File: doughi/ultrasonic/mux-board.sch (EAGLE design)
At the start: 34 parts, among them U1 TLV70233DBVR, X1 MINI-USB-UX60A-MB-5ST

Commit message: Made Schematic Neater
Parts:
- removed C8, C9: 1uF, rcl:C-USC0603
- removed POWER-LED: (no value), card:LEDSML0603
- removed R1: 10k, resistor:R-US_R0603
- removed R2: 1k, resistor:R-US_R0603
- removed SV1, SV10, SV11, SV12, SV13, SV14, SV15, SV16, SV2, SV3, SV4, SV5, SV6, SV7, SV8, SV9: (no value), mux-board:FE04-1
- removed U1: TLV70233DBVR, card:TLV70233DBVR
- added C10, C11: 1uF, rcl:C-USC0603
- added POWER-LED1: (no value), card:LEDSML0603
- added Q10, Q11, Q12, Q7, Q8, Q9: BSS138SMD, Logic_Level_Bidirectional:BSS138SMD
- added R15, R16, R17, R18, R19, R20, R21, R22, R23, R24, R25, R26: 10k, rcl:R-US_R0603
- added R3: 10k, resistor:R-US_R0603
- added R4: 1k, resistor:R-US_R0603
- added SV17, SV18, SV19, SV20, SV21, SV22, SV23, SV24, SV25, SV26, SV27, SV28, SV29, SV30, SV31, SV32: (no value), mux-board:FE04-1
- added U2: TLV70233DBVR, card:TLV70233DBVR
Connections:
- removed net N$3: R1.2, U1.EN
- removed net N$4: POWER-LED.C, R2.2
- new net ECHO_: Q12.S, R26.1, U$1.PA07/I7/AIN7/SERCOM0.3/I2SD0
- new net N$10: R3.2, U2.EN
- new net N$11: POWER-LED1.C, R4.2
- new net S0_: Q7.S, R16.1, U$1.PA02/EINT2/AIN0/Y0/VOUT
- new net S1_: Q8.S, R18.1, U$1.PA03/EINT3/VREFA/AIN1
- new net S2_: Q9.S, R20.1, U$1.PA04/EINT4/VREFB/AIN4/SERCOM0.0
- new net S3_: Q10.S, R22.1, U$1.PA05/EINT5/AIN5/SERCOM0.1
- new net TRIG_: Q11.S, R24.1, U$1.PA06/EINT6/AIN6/SERCOM0.2
- net +3.3V: now also C11.1, Q10.G, Q11.G, Q12.G, Q7.G, Q8.G, Q9.G, R16.2, R18.2, R20.2, R22.2, R24.2, R26.2, U2.VOUT; no longer C9.1, U1.VOUT
- net +5V: now also C10.1, POWER-LED1.A, R15.2, R17.2, R19.2, R21.2, R23.2, R25.2, R3.1, SV17.4, SV18.4, SV19.4, SV20.4, SV21.4, SV22.4, SV23.4, SV24.4, SV25.4, SV26.4, SV27.4, SV28.4, SV29.4, SV30.4, SV31.4, SV32.4, U2.VIN; no longer C8.1, POWER-LED.A, R1.1, SV1.4, SV10.4, SV11.4, SV12.4, SV13.4, SV14.4, SV15.4, SV16.4, SV2.4, SV3.4, SV4.4, SV5.4, SV6.4, SV7.4, SV8.4, SV9.4, U1.VIN
- net E0: now also SV17.2; no longer SV1.2
- net E1: now also SV18.2; no longer SV2.2
- net E10: now also SV27.2; no longer SV11.2
- net E11: now also SV28.2; no longer SV12.2
- net E12: now also SV29.2; no longer SV13.2
- net E13: now also SV30.2; no longer SV14.2
- net E14: now also SV31.2; no longer SV15.2
- net E15: now also SV32.2; no longer SV16.2
- net E2: now also SV19.2; no longer SV3.2
- net E3: now also SV20.2; no longer SV4.2
- net E4: now also SV21.2; no longer SV5.2
- net E5: now also SV22.2; no longer SV6.2
- net E6: now also SV23.2; no longer SV7.2
- net E7: now also SV24.2; no longer SV8.2
- net E8: now also SV25.2; no longer SV9.2
- net E9: now also SV26.2; no longer SV10.2
- net ECHO: now also Q12.D, R25.1; no longer U$1.PA07/I7/AIN7/SERCOM0.3/I2SD0
- net GND: now also C10.2, C11.2, R4.1, SV17.1, SV18.1, SV19.1, SV20.1, SV21.1, SV22.1, SV23.1, SV24.1, SV25.1, SV26.1, SV27.1, SV28.1, SV29.1, SV30.1, SV31.1, SV32.1, U2.GND; no longer C8.2, C9.2, R2.1, SV1.1, SV10.1, SV11.1, SV12.1, SV13.1, SV14.1, SV15.1, SV16.1, SV2.1, SV3.1, SV4.1, SV5.1, SV6.1, SV7.1, SV8.1, SV9.1, U1.GND
- net S0: now also Q7.D, R15.1; no longer U$1.PA02/EINT2/AIN0/Y0/VOUT
- net S1: now also Q8.D, R17.1; no longer U$1.PA03/EINT3/VREFA/AIN1
- net S2: now also Q9.D, R19.1; no longer U$1.PA04/EINT4/VREFB/AIN4/SERCOM0.0
- net S3: now also Q10.D, R21.1; no longer U$1.PA05/EINT5/AIN5/SERCOM0.1
- net T0: now also SV17.3; no longer SV1.3
- net T1: now also SV18.3; no longer SV2.3
- net T10: now also SV27.3; no longer SV11.3
- net T11: now also SV28.3; no longer SV12.3
- net T12: now also SV29.3; no longer SV13.3
- net T13: now also SV30.3; no longer SV14.3
- net T14: now also SV31.3; no longer SV15.3
- net T15: now also SV32.3; no longer SV16.3
- net T2: now also SV19.3; no longer SV3.3
- net T3: now also SV20.3; no longer SV4.3
- net T4: now also SV21.3; no longer SV5.3
- net T5: now also SV22.3; no longer SV6.3
- net T6: now also SV23.3; no longer SV7.3
- net T7: now also SV24.3; no longer SV8.3
- net T8: now also SV25.3; no longer SV9.3
- net T9: now also SV26.3; no longer SV10.3
- net TRIG: now also Q11.D, R23.1; no longer U$1.PA06/EINT6/AIN6/SERCOM0.2
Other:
- note added: "Level Shifters"
- note added: "Microcontroller"
- note added: "Multiplexors"
- note added: "Sensor Connectors"
- note added: "USB Connector"
- note added: "Voltage Regulator and Power Light"

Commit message: Ultrasonic Mux Board Pre-Review
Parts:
- removed C7: 10 uF, resistor:C-USC0603
- removed SV17, SV18, SV19, SV20, SV21, SV22, SV23, SV24, SV25, SV26, SV27, SV28, SV29, SV30, SV31, SV32: (no value), mux-board:FE04-1
- added C8: 1uF, rcl:C-USC0603
- added J1: B2P-VH(LF)(SN), RoboJackets-Connectors:B2P-VH(LF)(SN)
- added US1, US2, US3, US4, US5, US6, US7, US8: 4-PIN_2MM-H, RoboJackets-Connectors:4-PIN_2MM-H
- added US10, US11, US12, US13, US14, US15, US16, US9: 4-PIN_2MM-V, RoboJackets-Connectors:4-PIN_2MM-V
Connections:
- net +5V: now also C8.1, J1.1, US1.4, US10.4, US11.4, US12.4, US13.4, US14.4, US15.4, US16.4, US2.4, US3.4, US4.4, US5.4, US6.4, US7.4, US8.4, US9.4; no longer C7.1, SV17.4, SV18.4, SV19.4, SV20.4, SV21.4, SV22.4, SV23.4, SV24.4, SV25.4, SV26.4, SV27.4, SV28.4, SV29.4, SV30.4, SV31.4, SV32.4
- net E0: now also US1.2; no longer SV17.2
- net E1: now also US2.2; no longer SV18.2
- net E10: now also US11.2; no longer SV27.2
- net E11: now also US12.2; no longer SV28.2
- net E12: now also US13.2; no longer SV29.2
- net E13: now also US14.2; no longer SV30.2
- net E14: now also US15.2; no longer SV31.2
- net E15: now also US16.2; no longer SV32.2
- net E2: now also US3.2; no longer SV19.2
- net E3: now also US4.2; no longer SV20.2
- net E4: now also US5.2; no longer SV21.2
- net E5: now also US6.2; no longer SV22.2
- net E6: now also US7.2; no longer SV23.2
- net E7: now also US8.2; no longer SV24.2
- net E8: now also US9.2; no longer SV25.2
- net E9: now also US10.2; no longer SV26.2
- net GND: now also C8.2, J1.2, US1.1, US10.1, US11.1, US12.1, US13.1, US14.1, US15.1, US16.1, US2.1, US3.1, US4.1, US5.1, US6.1, US7.1, US8.1, US9.1; no longer C7.2, SV17.1, SV18.1, SV19.1, SV20.1, SV21.1, SV22.1, SV23.1, SV24.1, SV25.1, SV26.1, SV27.1, SV28.1, SV29.1, SV30.1, SV31.1, SV32.1
- net T0: now also US1.3; no longer SV17.3
- net T1: now also US2.3; no longer SV18.3
- net T10: now also US11.3; no longer SV27.3
- net T11: now also US12.3; no longer SV28.3
- net T12: now also US13.3; no longer SV29.3
- net T13: now also US14.3; no longer SV30.3
- net T14: now also US15.3; no longer SV31.3
- net T15: now also US16.3; no longer SV32.3
- net T2: now also US3.3; no longer SV19.3
- net T3: now also US4.3; no longer SV20.3
- net T4: now also US5.3; no longer SV21.3
- net T5: now also US6.3; no longer SV22.3
- net T6: now also US7.3; no longer SV23.3
- net T7: now also US8.3; no longer SV24.3
- net T8: now also US9.3; no longer SV25.3
- net T9: now also US10.3; no longer SV26.3
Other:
- note added: "Power Source/Indicator LED"
- note added: "Voltage Regulator"
- note removed: "Voltage Regulator and Power Light"
- moved on the sheet: C10, C11, POWER-LED1, R3, R4, U2

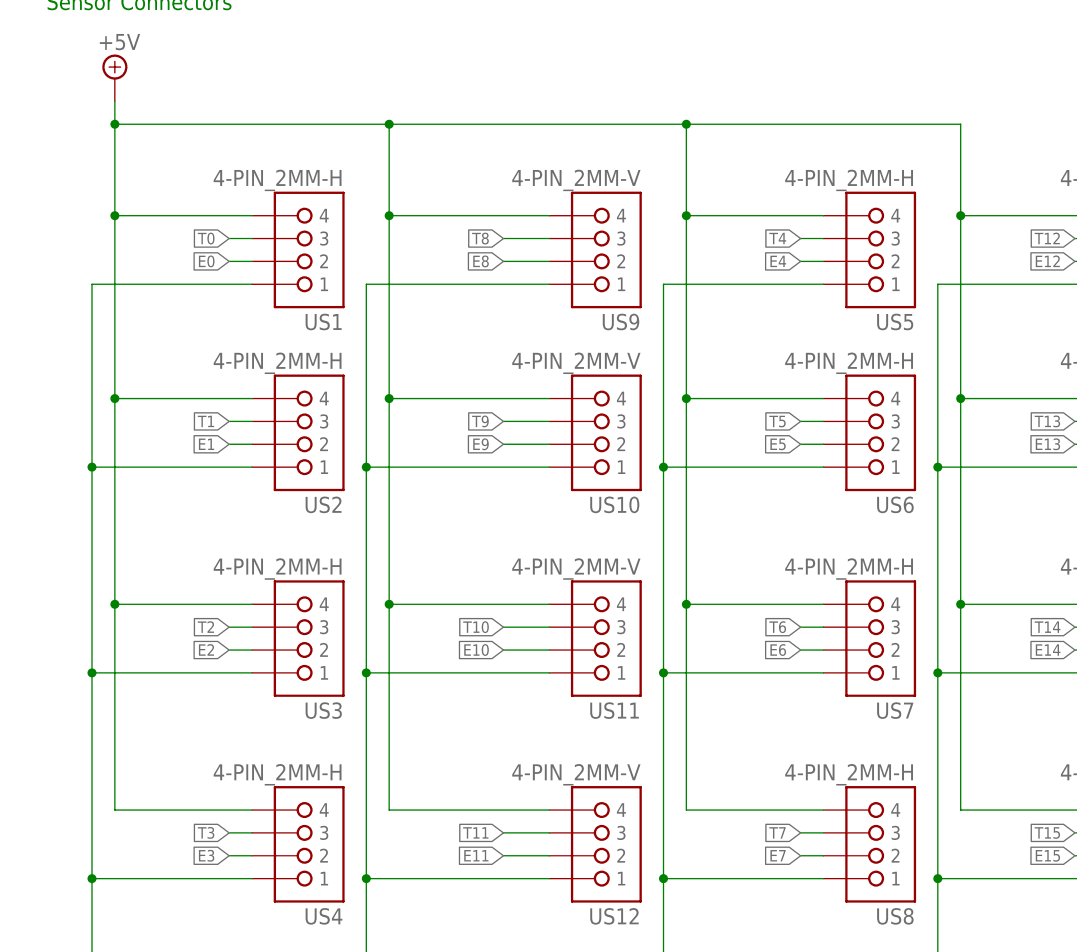
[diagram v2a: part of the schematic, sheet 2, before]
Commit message: Finished routing Ultrasonic board
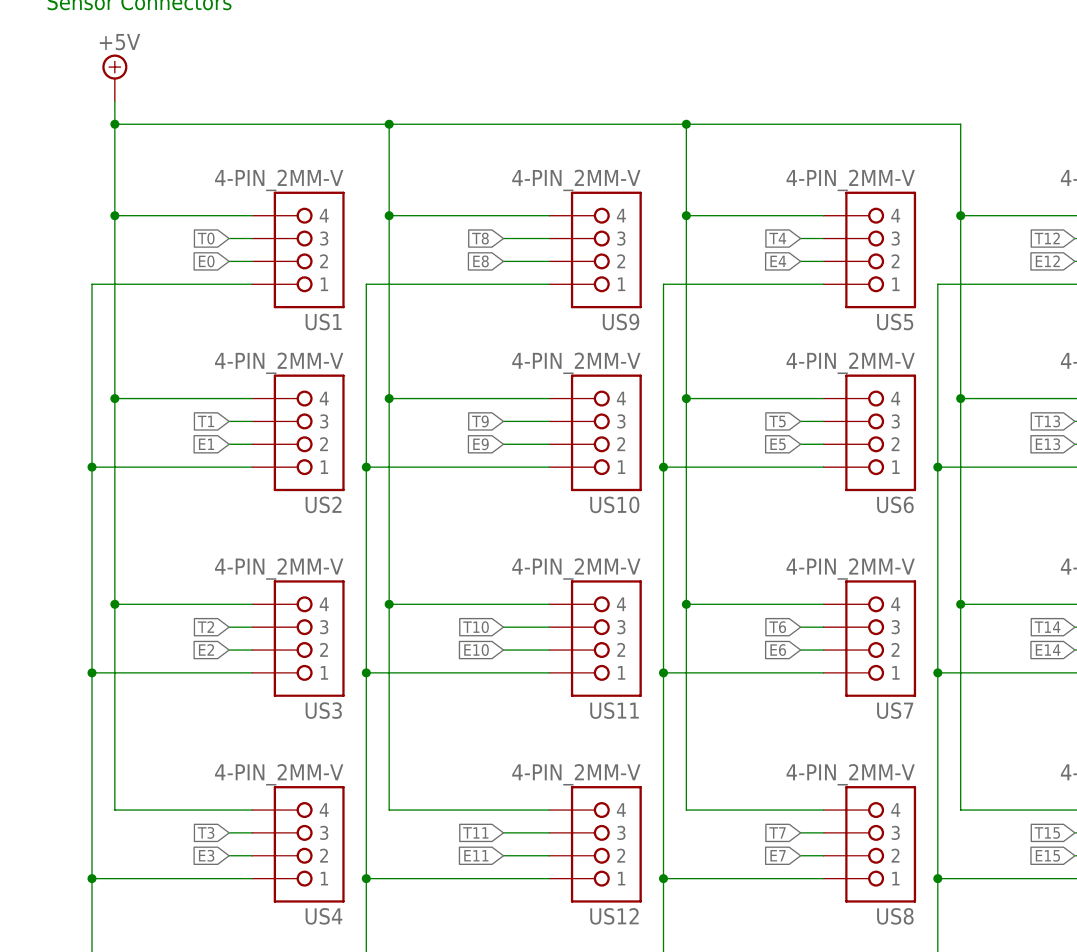
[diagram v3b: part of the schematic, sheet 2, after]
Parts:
- U$1: value ATSAMD21J_QFN -> ATSAMD21J_QFP; device card:ATSAMD21J_QFN -> mux-board:ATSAMD21J_QFP
- US1, US2, US3, US4, US5, US6, US7, US8: value 4-PIN_2MM-H -> 4-PIN_2MM-V; device RoboJackets-Connectors:4-PIN_2MM-H -> RoboJackets-Connectors:4-PIN_2MM-V
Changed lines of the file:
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@@
 </classes>
 <parts>
-<part name="U$1" library="card" deviceset="ATSAMD21J" device="_QFN"/>
+<part name="U$1" library="mux-board" deviceset="ATSAMD21J" device="_QFP"/>
 <part name="U$2" library="card" deviceset="PTS645SK50SMTR92" device=""/>
 <part name="SUPPLY1" library="supply2" library_urn="urn:adsk.eagle:library:372" deviceset="GND" device=""/>
@@
 <part name="SUPPLY12" library="supply2" library_urn="urn:adsk.eagle:library:372" deviceset="+5V" device=""/>
 <part name="FRAME2" library="frames" library_urn="urn:adsk.eagle:library:229" deviceset="A4L-LOC" device=""/>
-<part name="US1" library="RoboJackets-Connectors" deviceset="4-PIN_2MM-*" device="H"/>
-<part name="US2" library="RoboJackets-Connectors" deviceset="4-PIN_2MM-*" device="H"/>
-<part name="US3" library="RoboJackets-Connectors" deviceset="4-PIN_2MM-*" device="H"/>
-<part name="US4" library="RoboJackets-Connectors" deviceset="4-PIN_2MM-*" device="H"/>
-<part name="US5" library="RoboJackets-Connectors" deviceset="4-PIN_2MM-*" device="H"/>
-<part name="US6" library="RoboJackets-Connectors" deviceset="4-PIN_2MM-*" device="H"/>
-<part name="US7" library="RoboJackets-Connectors" deviceset="4-PIN_2MM-*" device="H"/>
-<part name="US8" library="RoboJackets-Connectors" deviceset="4-PIN_2MM-*" device="H"/>
+<part name="US1" library="RoboJackets-Connectors" deviceset="4-PIN_2MM-*" device="V" value="4-PIN_2MM-V"/>
+<part name="US2" library="RoboJackets-Connectors" deviceset="4-PIN_2MM-*" device="V" value="4-PIN_2MM-V"/>
+<part name="US3" library="RoboJackets-Connectors" deviceset="4-PIN_2MM-*" device="V" value="4-PIN_2MM-V"/>
+<part name="US4" library="RoboJackets-Connectors" deviceset="4-PIN_2MM-*" device="V" value="4-PIN_2MM-V"/>
+<part name="US5" library="RoboJackets-Connectors" deviceset="4-PIN_2MM-*" device="V" value="4-PIN_2MM-V"/>
+<part name="US6" library="RoboJackets-Connectors" deviceset="4-PIN_2MM-*" device="V" value="4-PIN_2MM-V"/>
+<part name="US7" library="RoboJackets-Connectors" deviceset="4-PIN_2MM-*" device="V" value="4-PIN_2MM-V"/>
+<part name="US8" library="RoboJackets-Connectors" deviceset="4-PIN_2MM-*" device="V" value="4-PIN_2MM-V"/>
 <part name="US9" library="RoboJackets-Connectors" deviceset="4-PIN_2MM-*" device="V" value="4-PIN_2MM-V"/>
 <part name="US10" library="RoboJackets-Connectors" deviceset="4-PIN_2MM-*" device="V" value="4-PIN_2MM-V"/>

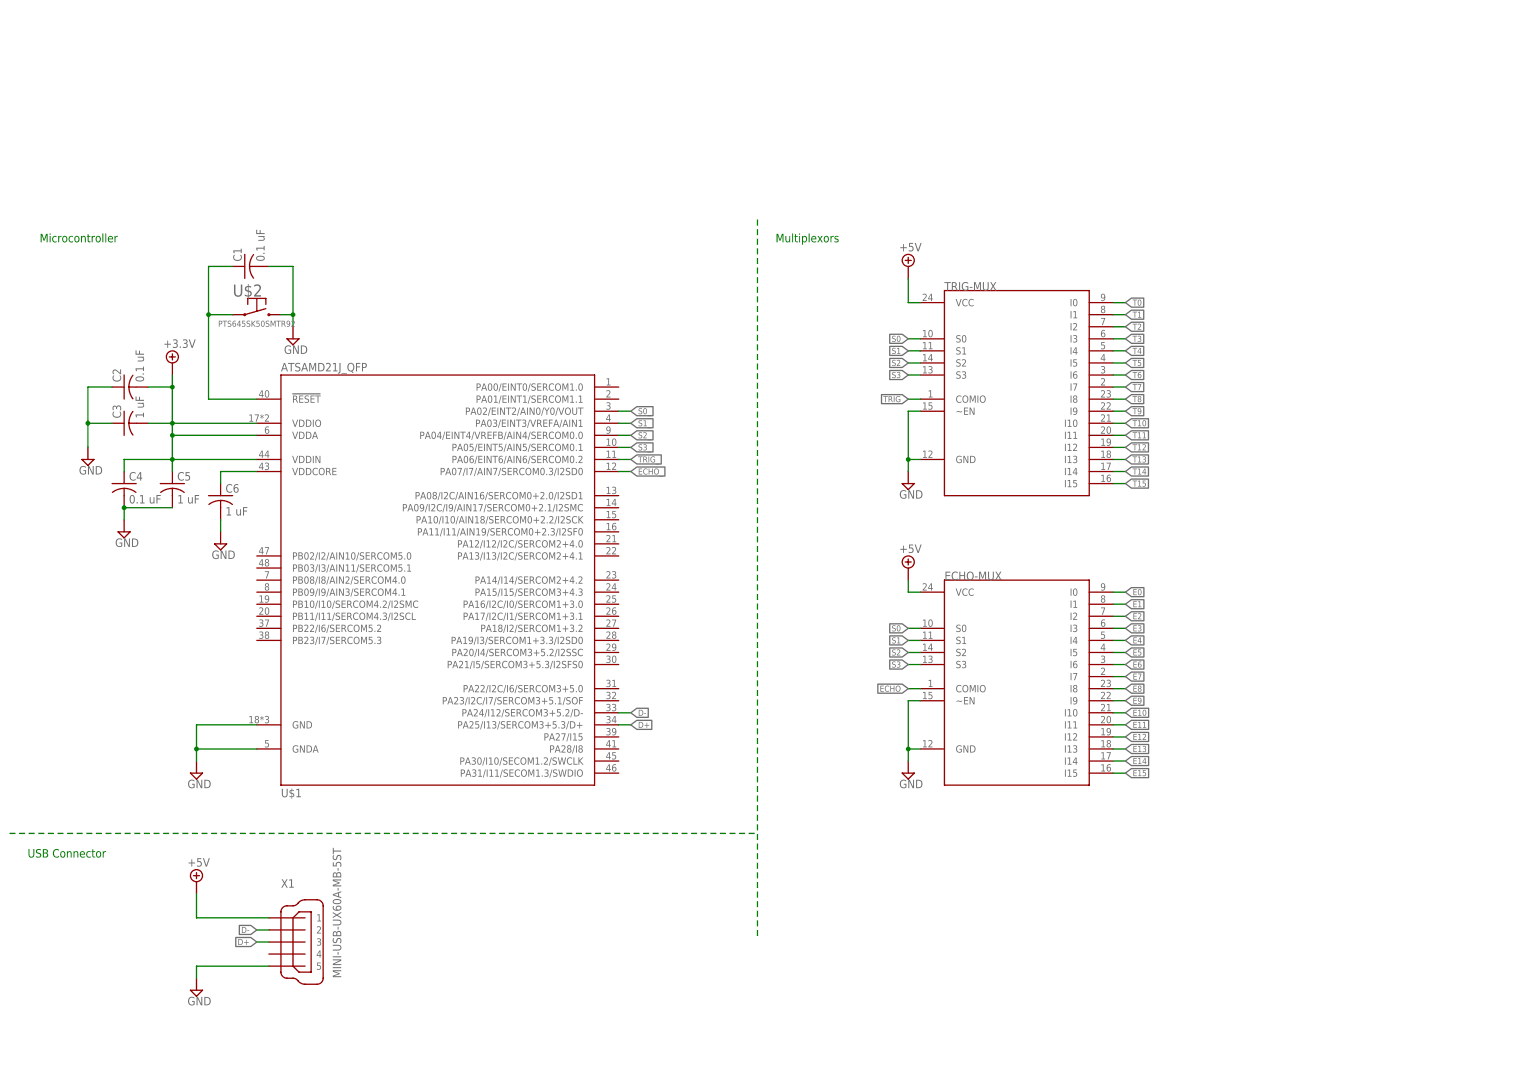
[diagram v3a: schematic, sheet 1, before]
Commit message: Made small routing changes to the mux board
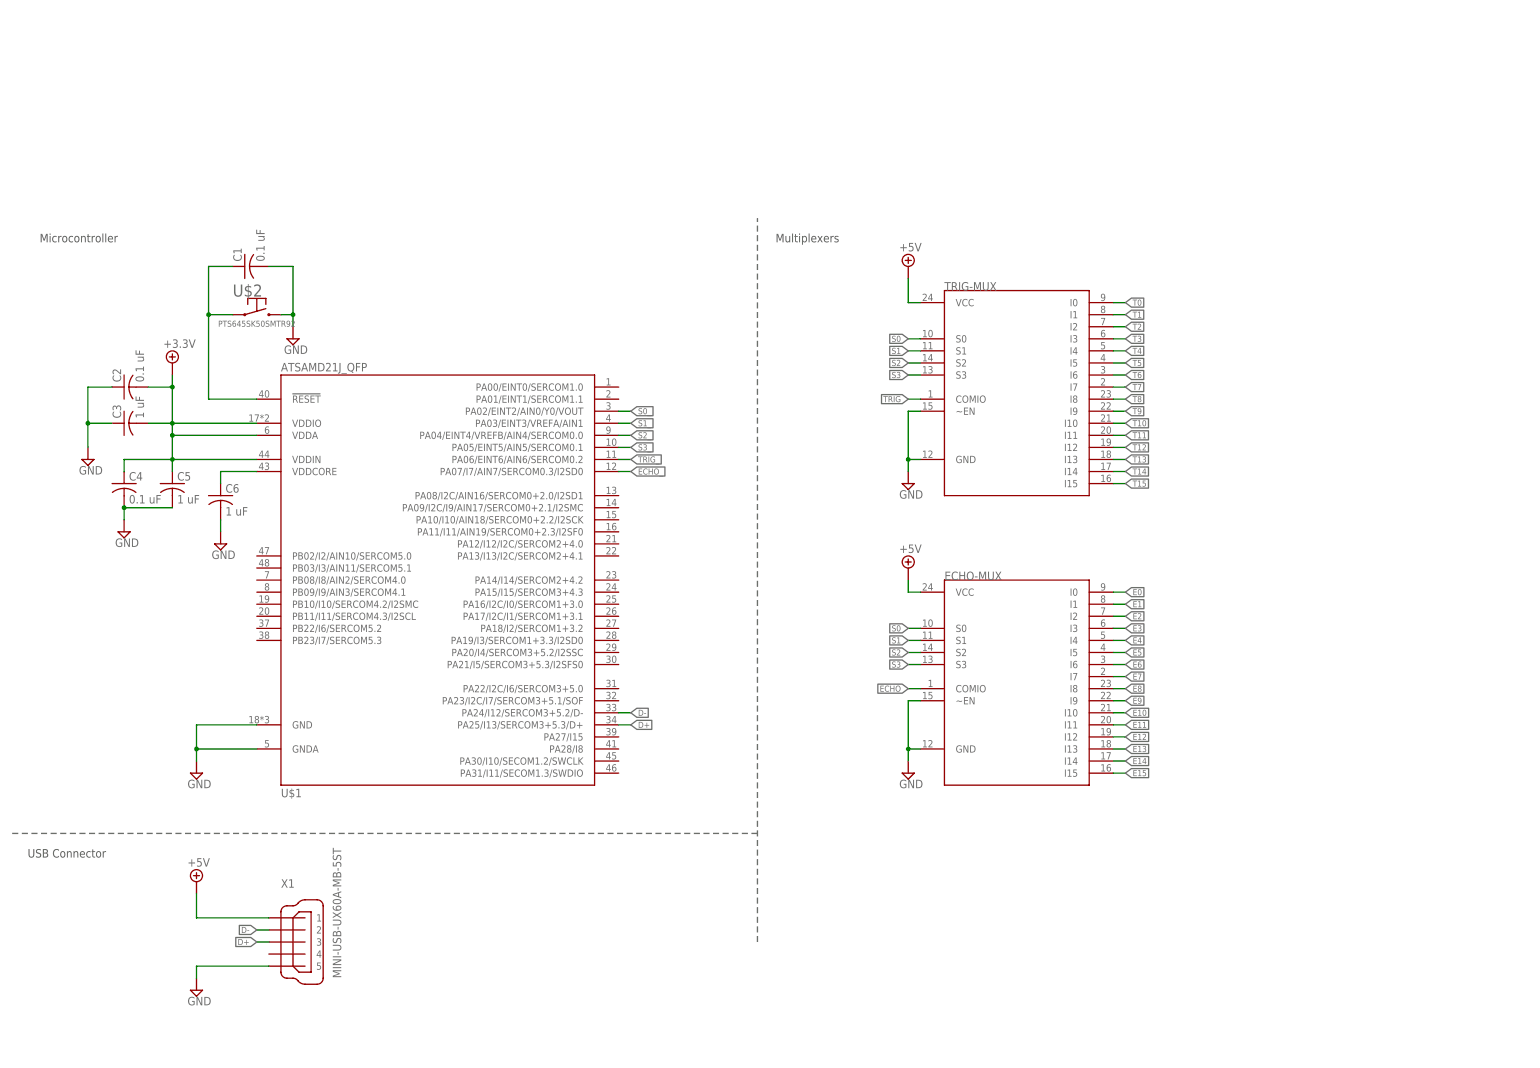
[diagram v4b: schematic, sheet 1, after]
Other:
- note added: "Multiplexers"
- note removed: "Multiplexors"
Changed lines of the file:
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@@
 <?xml version="1.0" encoding="utf-8"?>
 <!DOCTYPE eagle SYSTEM "eagle.dtd">
-<eagle version="8.5.1">
+<eagle version="8.5.0">
 <drawing>
 <settings>
@@
 <layer number="95" name="Names" color="7" fill="1" visible="yes" active="yes"/>
 <layer number="96" name="Values" color="7" fill="1" visible="yes" active="yes"/>
-<layer number="97" name="Info" color="7" fill="1" visible="no" active="yes"/>
+<layer number="97" name="Info" color="7" fill="1" visible="yes" active="yes"/>
 <layer number="98" name="Guide" color="6" fill="1" visible="no" active="yes"/>
 <layer number="99" name="SpiceOrder" color="7" fill="1" visible="no" active="yes"/>
@@
 <sheet>
 <plain>
-<text x="10.16" y="170.18" size="1.778" layer="91">Microcontroller</text>
-<text x="165.1" y="170.18" size="1.778" layer="91">Multiplexors</text>
-<text x="7.62" y="40.64" size="1.778" layer="91">USB Connector</text>
+<text x="10.16" y="170.18" size="1.778" layer="97">Microcontroller</text>
+<text x="165.1" y="170.18" size="1.778" layer="97">Multiplexers</text>
+<text x="7.62" y="40.64" size="1.778" layer="97">USB Connector</text>
+<wire x1="161.29" y1="45.72" x2="3.8862" y2="45.72" width="0.1524" layer="97" style="shortdash"/>
+<wire x1="161.29" y1="22.86" x2="161.29" y2="175.26" width="0.1524" layer="97" style="shortdash"/>
 </plain>
 <instances>
@@
 </segment>
 </net>
-<net name="N$3" class="0">
-<segment>
-<wire x1="161.29" y1="24.13" x2="161.29" y2="175.26" width="0.1524" layer="91" style="shortdash"/>
-</segment>
-</net>
-<net name="N$4" class="0">
-<segment>
-<wire x1="3.81" y1="45.72" x2="161.29" y2="45.72" width="0.1524" layer="91" style="shortdash"/>
-</segment>
-</net>
 </nets>
 </sheet>
 <sheet>
 <plain>
-<text x="73.66" y="48.26" size="1.778" layer="91">Voltage Regulator</text>
-<text x="160.02" y="170.18" size="1.778" layer="91">Level Shifters</text>
-<text x="10.16" y="170.18" size="1.778" layer="91">Sensor Connectors</text>
-<text x="7.62" y="48.26" size="1.778" layer="91">Power Source/Indicator LED</text>
+<text x="73.66" y="48.26" size="1.778" layer="97">Voltage Regulator</text>
+<text x="160.02" y="170.18" size="1.778" layer="97">Level Shifters</text>
+<text x="10.16" y="170.18" size="1.778" layer="97">Sensor Connectors</text>
+<text x="7.62" y="48.26" size="1.778" layer="97">Power Source/Indicator LED</text>
 </plain>
 <instances>
